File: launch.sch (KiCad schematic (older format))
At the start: 24 parts, among them J15 CHARGE_A, J16 CHARGE_B, Q1 Q_NPN_BCE, Q2 Q_NMOS_DGS, Q3 Q_NPN_BCE, Q4 Q_NMOS_DGS

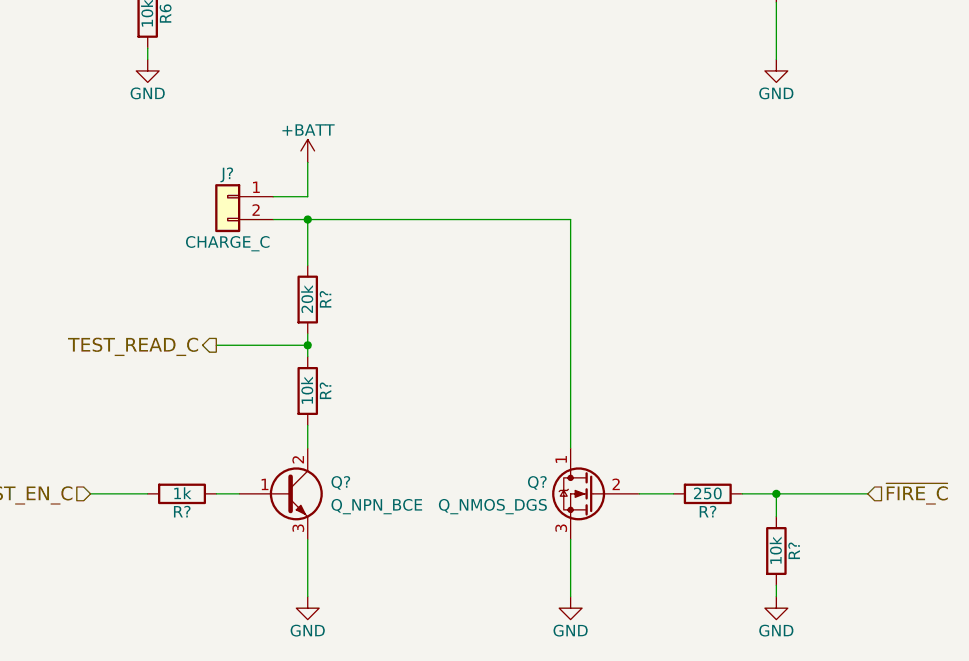
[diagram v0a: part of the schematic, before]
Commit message: added sd card
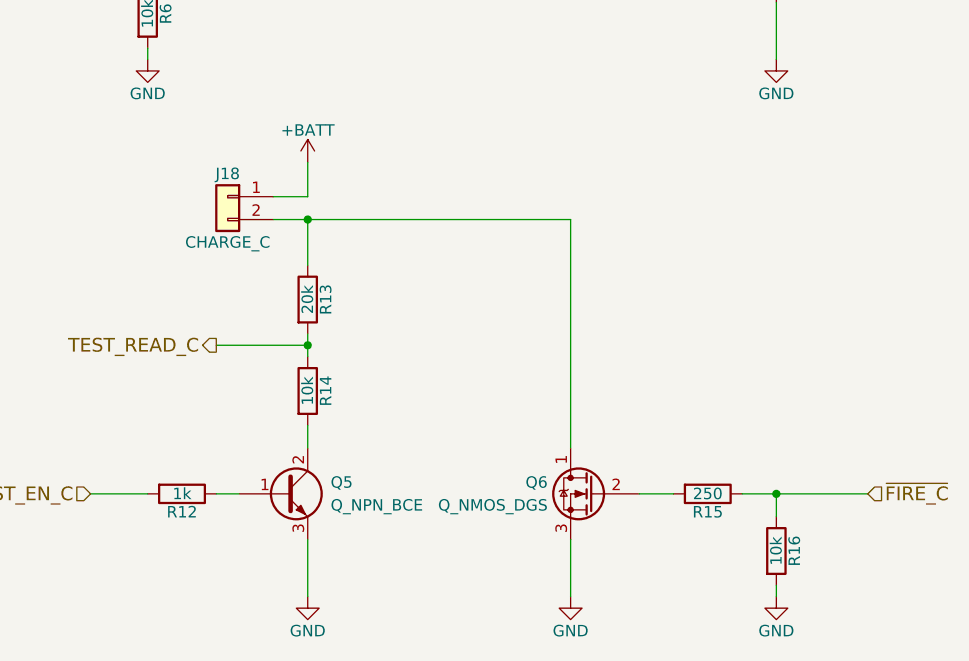
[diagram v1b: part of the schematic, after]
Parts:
- gave numbers to parts that had none: 8
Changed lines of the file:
@@
 LIBS:RFM95
 LIBS:TXB0104DR
+LIBS:LOGIC-TXS0108EPWR_TSSOP20_
 LIBS:Draco-cache
 EELAYER 25 0
@@
 $EndDescr
 $Comp
-L +BATT #PWR033
+L +BATT #PWR035
 U 1 1 5A5BE339
 P 2350 1600
-F 0 "#PWR033" H 2350 1450 50  0001 C CNN
+F 0 "#PWR035" H 2350 1450 50  0001 C CNN
 F 1 "+BATT" H 2350 1740 50  0000 C CNN
 F 2 "" H 2350 1600 50  0001 C CNN
@@
 $EndComp
 $Comp
-L GND #PWR034
+L GND #PWR036
 U 1 1 5A5BE533
 P 2350 3500
-F 0 "#PWR034" H 2350 3250 50  0001 C CNN
+F 0 "#PWR036" H 2350 3250 50  0001 C CNN
 F 1 "GND" H 2350 3350 50  0000 C CNN
 F 2 "" H 2350 3500 50  0001 C CNN
@@
 	3500 3250 3500 3500
 $Comp
-L GND #PWR035
+L GND #PWR037
 U 1 1 5A5BF84A
 P 3500 3500
-F 0 "#PWR035" H 3500 3250 50  0001 C CNN
+F 0 "#PWR037" H 3500 3250 50  0001 C CNN
 F 1 "GND" H 3500 3350 50  0000 C CNN
 F 2 "" H 3500 3500 50  0001 C CNN
@@
 $EndComp
 $Comp
-L GND #PWR036
+L GND #PWR038
 U 1 1 5A5BFA29
 P 4400 3500
-F 0 "#PWR036" H 4400 3250 50  0001 C CNN
+F 0 "#PWR038" H 4400 3250 50  0001 C CNN
 F 1 "GND" H 4400 3350 50  0000 C CNN
 F 2 "" H 4400 3500 50  0001 C CNN
@@
 ~FIRE_A
 $Comp
-L +BATT #PWR037
+L +BATT #PWR039
 U 1 1 5A5C03B4
 P 7150 1600
-F 0 "#PWR037" H 7150 1450 50  0001 C CNN
+F 0 "#PWR039" H 7150 1450 50  0001 C CNN
 F 1 "+BATT" H 7150 1740 50  0000 C CNN
 F 2 "" H 7150 1600 50  0001 C CNN
@@
 $EndComp
 $Comp
-L GND #PWR038
+L GND #PWR040
 U 1 1 5A5C03DC
 P 7150 3500
-F 0 "#PWR038" H 7150 3250 50  0001 C CNN
+F 0 "#PWR040" H 7150 3250 50  0001 C CNN
 F 1 "GND" H 7150 3350 50  0000 C CNN
 F 2 "" H 7150 3500 50  0001 C CNN
@@
 	8300 3250 8300 3500
 $Comp
-L GND #PWR039
+L GND #PWR041
 U 1 1 5A5C03F2
 P 8300 3500
-F 0 "#PWR039" H 8300 3250 50  0001 C CNN
+F 0 "#PWR041" H 8300 3250 50  0001 C CNN
 F 1 "GND" H 8300 3350 50  0000 C CNN
 F 2 "" H 8300 3500 50  0001 C CNN
@@
 $EndComp
 $Comp
-L GND #PWR040
+L GND #PWR042
 U 1 1 5A5C040E
 P 9200 3500
-F 0 "#PWR040" H 9200 3250 50  0001 C CNN
+F 0 "#PWR042" H 9200 3250 50  0001 C CNN
 F 1 "GND" H 9200 3350 50  0000 C CNN
 F 2 "" H 9200 3500 50  0001 C CNN
@@
 Connection ~ 9200 3050
 $Comp
-L +BATT #PWR041
+L +BATT #PWR043
 U 1 1 5A5C9AE9
 P 5100 3950
-F 0 "#PWR041" H 5100 3800 50  0001 C CNN
+F 0 "#PWR043" H 5100 3800 50  0001 C CNN
 F 1 "+BATT" H 5100 4090 50  0000 C CNN
 F 2 "" H 5100 3950 50  0001 C CNN
@@
 $EndComp
 $Comp
-L Conn_01x02 J?
+L Conn_01x02 J18
 U 1 1 5A5C9AEF
 P 4750 4100
-F 0 "J?" H 4750 4200 50  0000 C CNN
+F 0 "J18" H 4750 4200 50  0000 C CNN
 F 1 "CHARGE_C" H 4750 3900 50  0000 C CNN
 F 2 "" H 4750 4100 50  0001 C CNN
@@
 	4950 4200 6250 4200
 $Comp
-L R R?
+L R R13
 U 1 1 5A5C9AF9
 P 5100 4550
-F 0 "R?" V 5180 4550 50  0000 C CNN
+F 0 "R13" V 5180 4550 50  0000 C CNN
 F 1 "20k" V 5100 4550 50  0000 C CNN
 F 2 "" V 5030 4550 50  0001 C CNN
@@
 $EndComp
 $Comp
-L R R?
+L R R14
 U 1 1 5A5C9AFF
 P 5100 4950
-F 0 "R?" V 5180 4950 50  0000 C CNN
+F 0 "R14" V 5180 4950 50  0000 C CNN
 F 1 "10k" V 5100 4950 50  0000 C CNN
 F 2 "" V 5030 4950 50  0001 C CNN
@@
 $EndComp
 $Comp
-L R R?
+L R R12
 U 1 1 5A5C9B05
 P 4550 5400
-F 0 "R?" V 4630 5400 50  0000 C CNN
+F 0 "R12" V 4630 5400 50  0000 C CNN
 F 1 "1k" V 4550 5400 50  0000 C CNN
 F 2 "" V 4480 5400 50  0001 C CNN
@@
 $EndComp
 $Comp
-L Q_NPN_BCE Q?
+L Q_NPN_BCE Q5
 U 1 1 5A5C9B0B
 P 5000 5400
-F 0 "Q?" H 5200 5450 50  0000 L CNN
+F 0 "Q5" H 5200 5450 50  0000 L CNN
 F 1 "Q_NPN_BCE" H 5200 5350 50  0000 L CNN
 F 2 "" H 5200 5500 50  0001 C CNN
@@
 $EndComp
 $Comp
-L GND #PWR042
+L GND #PWR044
 U 1 1 5A5C9B11
 P 5100 5850
-F 0 "#PWR042" H 5100 5600 50  0001 C CNN
+F 0 "#PWR044" H 5100 5600 50  0001 C CNN
 F 1 "GND" H 5100 5700 50  0000 C CNN
 F 2 "" H 5100 5850 50  0001 C CNN
@@
 TEST_READ_C
 $Comp
-L Q_NMOS_DGS Q?
+L Q_NMOS_DGS Q6
 U 1 1 5A5C9B20
 P 6350 5400
-F 0 "Q?" H 6550 5450 50  0000 L CNN
+F 0 "Q6" H 6550 5450 50  0000 L CNN
 F 1 "Q_NMOS_DGS" H 6550 5350 50  0000 L CNN
 F 2 "" H 6550 5500 50  0001 C CNN
@@
 	6250 5600 6250 5850
 $Comp
-L GND #PWR043
+L GND #PWR045
 U 1 1 5A5C9B27
 P 6250 5850
-F 0 "#PWR043" H 6250 5600 50  0001 C CNN
+F 0 "#PWR045" H 6250 5600 50  0001 C CNN
 F 1 "GND" H 6250 5700 50  0000 C CNN
 F 2 "" H 6250 5850 50  0001 C CNN
@@
 Connection ~ 5100 4200
 $Comp
-L R R?
+L R R16
 U 1 1 5A5C9B2F
 P 7150 5650
-F 0 "R?" V 7230 5650 50  0000 C CNN
+F 0 "R16" V 7230 5650 50  0000 C CNN
 F 1 "10k" V 7150 5650 50  0000 C CNN
 F 2 "" V 7080 5650 50  0001 C CNN
@@
 $EndComp
 $Comp
-L GND #PWR044
+L GND #PWR046
 U 1 1 5A5C9B35
 P 7150 5850
-F 0 "#PWR044" H 7150 5600 50  0001 C CNN
+F 0 "#PWR046" H 7150 5600 50  0001 C CNN
 F 1 "GND" H 7150 5700 50  0000 C CNN
 F 2 "" H 7150 5850 50  0001 C CNN
@@
 	7150 5850 7150 5800
 $Comp
-L R R?
+L R R15
 U 1 1 5A5C9B3C
 P 6850 5400
-F 0 "R?" V 6930 5400 50  0000 C CNN
+F 0 "R15" V 6930 5400 50  0000 C CNN
 F 1 "250" V 6850 5400 50  0000 C CNN
 F 2 "" V 6780 5400 50  0001 C CNN

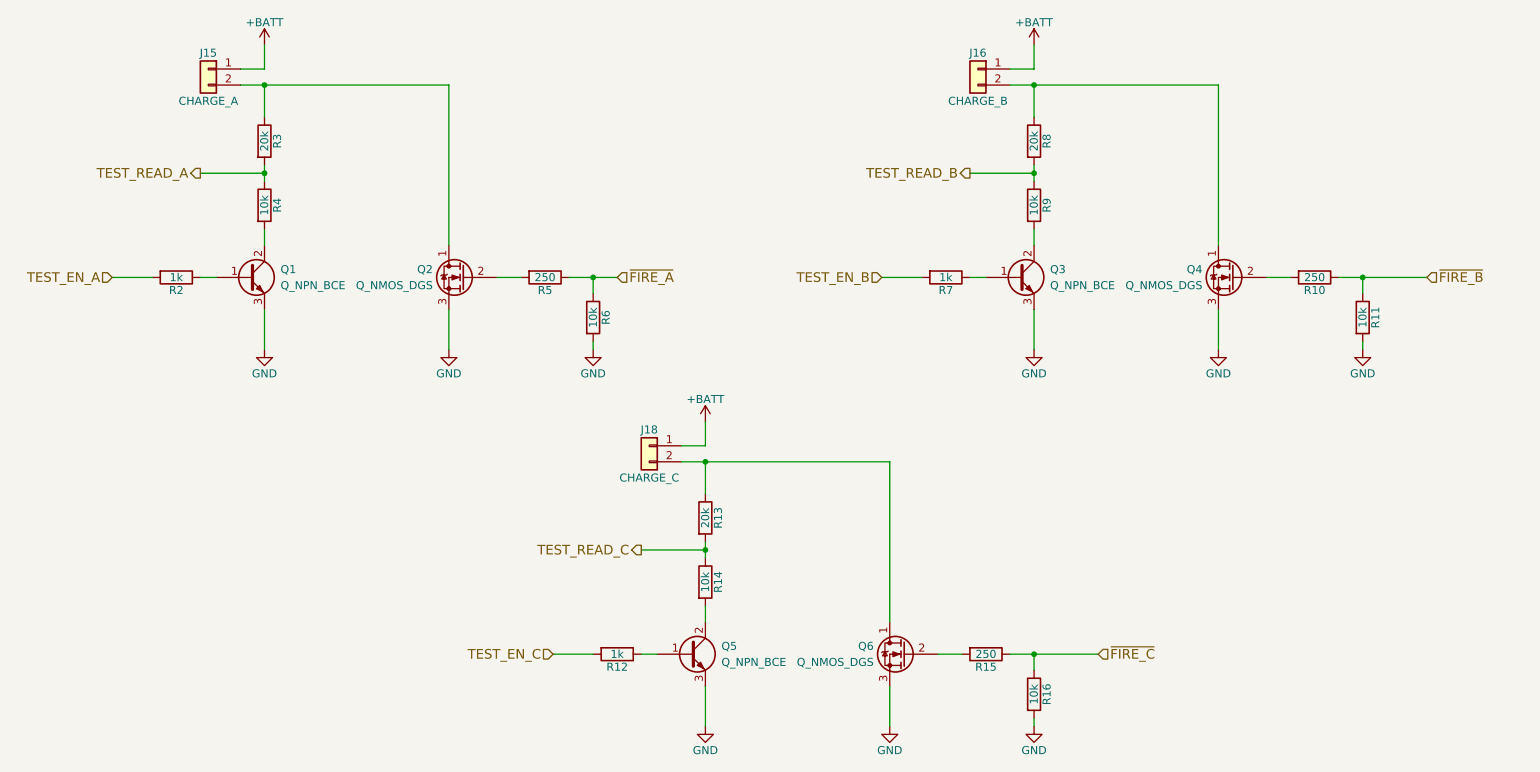
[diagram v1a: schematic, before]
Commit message: Did design review. Changed/confirmed voltage levels
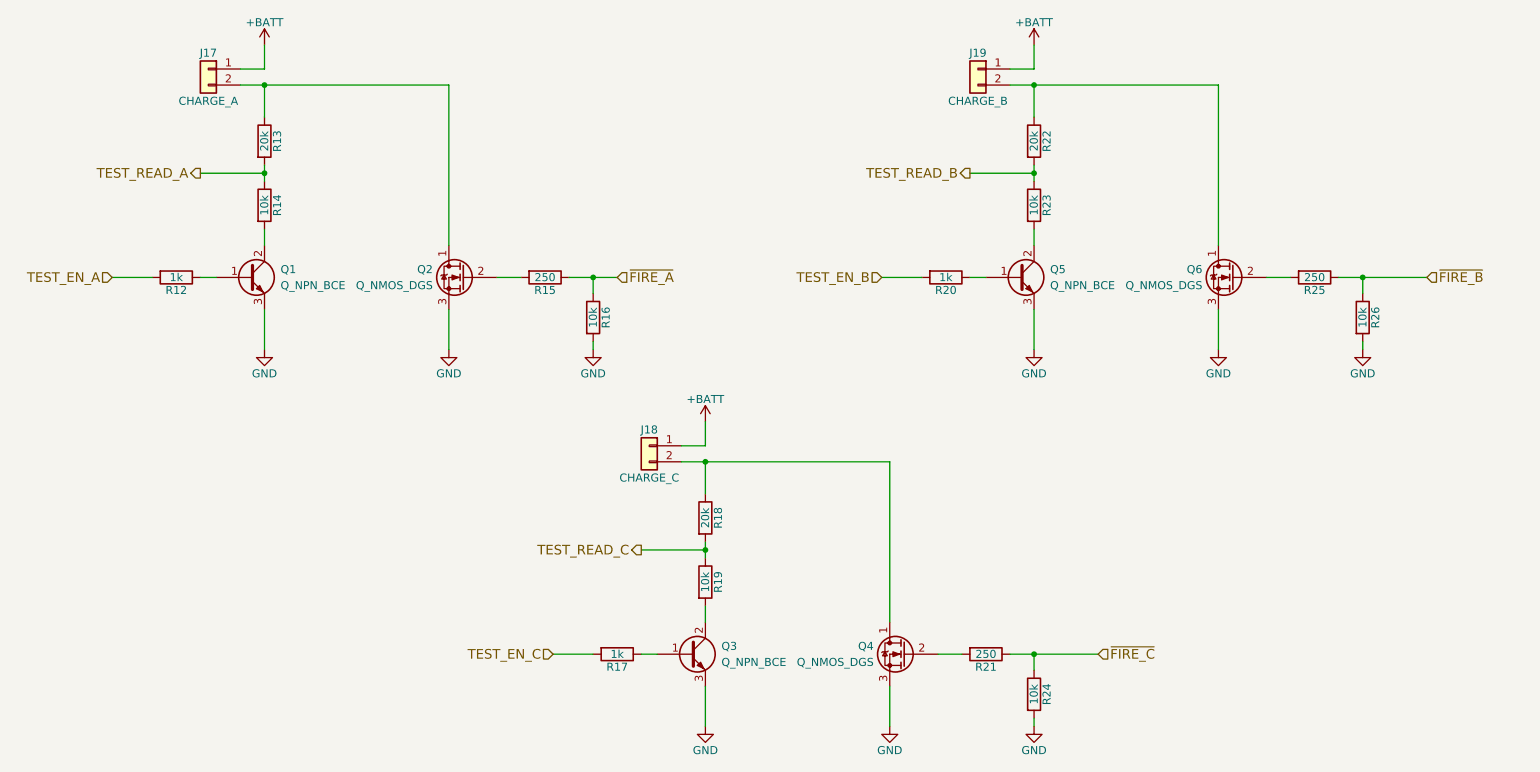
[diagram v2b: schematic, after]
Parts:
- R12: renamed from R2; footprint (none) -> Resistors_SMD:R_0805
- R13: renamed from R3; footprint (none) -> Resistors_SMD:R_0805
- R14: renamed from R4; footprint (none) -> Resistors_SMD:R_0805
- R15: renamed from R5; footprint (none) -> Resistors_SMD:R_0805
- R16: renamed from R6; footprint (none) -> Resistors_SMD:R_0805
- R17: renamed from R12; footprint (none) -> Resistors_SMD:R_0805
- R18: renamed from R13; footprint (none) -> Resistors_SMD:R_0805
- R19: renamed from R14; footprint (none) -> Resistors_SMD:R_0805
- R20: renamed from R7; footprint (none) -> Resistors_SMD:R_0805
- R21: renamed from R15; footprint (none) -> Resistors_SMD:R_0805
- R22: renamed from R8; footprint (none) -> Resistors_SMD:R_0805
- R23: renamed from R9; footprint (none) -> Resistors_SMD:R_0805
- R24: renamed from R16; footprint (none) -> Resistors_SMD:R_0805
- R25: renamed from R10; footprint (none) -> Resistors_SMD:R_0805
- R26: renamed from R11; footprint (none) -> Resistors_SMD:R_0805
- renumbered J15 to J17, J16 to J19, Q5 to Q3, Q6 to Q4, Q3 to Q5, Q4 to Q6
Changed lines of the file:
@@
 $EndDescr
 $Comp
-L +BATT #PWR035
+L +BATT #PWR046
 U 1 1 5A5BE339
 P 2350 1600
-F 0 "#PWR035" H 2350 1450 50  0001 C CNN
+F 0 "#PWR046" H 2350 1450 50  0001 C CNN
 F 1 "+BATT" H 2350 1740 50  0000 C CNN
 F 2 "" H 2350 1600 50  0001 C CNN
@@
 $EndComp
 $Comp
-L Conn_01x02 J15
+L Conn_01x02 J17
 U 1 1 5A5BE34D
 P 2000 1750
-F 0 "J15" H 2000 1850 50  0000 C CNN
+F 0 "J17" H 2000 1850 50  0000 C CNN
 F 1 "CHARGE_A" H 2000 1550 50  0000 C CNN
 F 2 "" H 2000 1750 50  0001 C CNN
@@
 	2200 1850 3500 1850
 $Comp
-L R R3
+L R R13
 U 1 1 5A5BE412
 P 2350 2200
-F 0 "R3" V 2430 2200 50  0000 C CNN
+F 0 "R13" V 2430 2200 50  0000 C CNN
 F 1 "20k" V 2350 2200 50  0000 C CNN
-F 2 "" V 2280 2200 50  0001 C CNN
+F 2 "Resistors_SMD:R_0805" V 2280 2200 50  0001 C CNN
 F 3 "" H 2350 2200 50  0001 C CNN
 	1    2350 2200
@@
 $EndComp
 $Comp
-L R R4
+L R R14
 U 1 1 5A5BE487
 P 2350 2600
-F 0 "R4" V 2430 2600 50  0000 C CNN
+F 0 "R14" V 2430 2600 50  0000 C CNN
 F 1 "10k" V 2350 2600 50  0000 C CNN
-F 2 "" V 2280 2600 50  0001 C CNN
+F 2 "Resistors_SMD:R_0805" V 2280 2600 50  0001 C CNN
 F 3 "" H 2350 2600 50  0001 C CNN
 	1    2350 2600
@@
 $EndComp
 $Comp
-L R R2
+L R R12
 U 1 1 5A5BE4BA
 P 1800 3050
-F 0 "R2" V 1880 3050 50  0000 C CNN
+F 0 "R12" V 1880 3050 50  0000 C CNN
 F 1 "1k" V 1800 3050 50  0000 C CNN
-F 2 "" V 1730 3050 50  0001 C CNN
+F 2 "Resistors_SMD:R_0805" V 1730 3050 50  0001 C CNN
 F 3 "" H 1800 3050 50  0001 C CNN
 	1    1800 3050
@@
 $EndComp
 $Comp
-L GND #PWR036
+L GND #PWR047
 U 1 1 5A5BE533
 P 2350 3500
-F 0 "#PWR036" H 2350 3250 50  0001 C CNN
+F 0 "#PWR047" H 2350 3250 50  0001 C CNN
 F 1 "GND" H 2350 3350 50  0000 C CNN
 F 2 "" H 2350 3500 50  0001 C CNN
@@
 	3500 3250 3500 3500
 $Comp
-L GND #PWR037
+L GND #PWR048
 U 1 1 5A5BF84A
 P 3500 3500
-F 0 "#PWR037" H 3500 3250 50  0001 C CNN
+F 0 "#PWR048" H 3500 3250 50  0001 C CNN
 F 1 "GND" H 3500 3350 50  0000 C CNN
 F 2 "" H 3500 3500 50  0001 C CNN
@@
 Connection ~ 2350 1850
 $Comp
-L R R6
+L R R16
 U 1 1 5A5BF9CA
 P 4400 3300
-F 0 "R6" V 4480 3300 50  0000 C CNN
+F 0 "R16" V 4480 3300 50  0000 C CNN
 F 1 "10k" V 4400 3300 50  0000 C CNN
-F 2 "" V 4330 3300 50  0001 C CNN
+F 2 "Resistors_SMD:R_0805" V 4330 3300 50  0001 C CNN
 F 3 "" H 4400 3300 50  0001 C CNN
 	1    4400 3300
@@
 $EndComp
 $Comp
-L GND #PWR038
+L GND #PWR049
 U 1 1 5A5BFA29
 P 4400 3500
-F 0 "#PWR038" H 4400 3250 50  0001 C CNN
+F 0 "#PWR049" H 4400 3250 50  0001 C CNN
 F 1 "GND" H 4400 3350 50  0000 C CNN
 F 2 "" H 4400 3500 50  0001 C CNN
@@
 	4400 3500 4400 3450
 $Comp
-L R R5
+L R R15
 U 1 1 5A5BFB6E
 P 4100 3050
-F 0 "R5" V 4180 3050 50  0000 C CNN
+F 0 "R15" V 4180 3050 50  0000 C CNN
 F 1 "250" V 4100 3050 50  0000 C CNN
-F 2 "" V 4030 3050 50  0001 C CNN
+F 2 "Resistors_SMD:R_0805" V 4030 3050 50  0001 C CNN
 F 3 "" H 4100 3050 50  0001 C CNN
 	1    4100 3050
@@
 ~FIRE_A
 $Comp
-L +BATT #PWR039
+L +BATT #PWR050
 U 1 1 5A5C03B4
 P 7150 1600
-F 0 "#PWR039" H 7150 1450 50  0001 C CNN
+F 0 "#PWR050" H 7150 1450 50  0001 C CNN
 F 1 "+BATT" H 7150 1740 50  0000 C CNN
 F 2 "" H 7150 1600 50  0001 C CNN
@@
 $EndComp
 $Comp
-L Conn_01x02 J16
+L Conn_01x02 J19
 U 1 1 5A5C03BA
 P 6800 1750
-F 0 "J16" H 6800 1850 50  0000 C CNN
+F 0 "J19" H 6800 1850 50  0000 C CNN
 F 1 "CHARGE_B" H 6800 1550 50  0000 C CNN
 F 2 "" H 6800 1750 50  0001 C CNN
@@
 	7000 1850 8300 1850
 $Comp
-L R R8
+L R R22
 U 1 1 5A5C03C4
 P 7150 2200
-F 0 "R8" V 7230 2200 50  0000 C CNN
+F 0 "R22" V 7230 2200 50  0000 C CNN
 F 1 "20k" V 7150 2200 50  0000 C CNN
-F 2 "" V 7080 2200 50  0001 C CNN
+F 2 "Resistors_SMD:R_0805" V 7080 2200 50  0001 C CNN
 F 3 "" H 7150 2200 50  0001 C CNN
 	1    7150 2200
@@
 $EndComp
 $Comp
-L R R9
+L R R23
 U 1 1 5A5C03CA
 P 7150 2600
-F 0 "R9" V 7230 2600 50  0000 C CNN
+F 0 "R23" V 7230 2600 50  0000 C CNN
 F 1 "10k" V 7150 2600 50  0000 C CNN
-F 2 "" V 7080 2600 50  0001 C CNN
+F 2 "Resistors_SMD:R_0805" V 7080 2600 50  0001 C CNN
 F 3 "" H 7150 2600 50  0001 C CNN
 	1    7150 2600
@@
 $EndComp
 $Comp
-L R R7
+L R R20
 U 1 1 5A5C03D0
 P 6600 3050
-F 0 "R7" V 6680 3050 50  0000 C CNN
+F 0 "R20" V 6680 3050 50  0000 C CNN
 F 1 "1k" V 6600 3050 50  0000 C CNN
-F 2 "" V 6530 3050 50  0001 C CNN
+F 2 "Resistors_SMD:R_0805" V 6530 3050 50  0001 C CNN
 F 3 "" H 6600 3050 50  0001 C CNN
 	1    6600 3050
@@
 $EndComp
 $Comp
-L Q_NPN_BCE Q3
+L Q_NPN_BCE Q5
 U 1 1 5A5C03D6
 P 7050 3050
-F 0 "Q3" H 7250 3100 50  0000 L CNN
+F 0 "Q5" H 7250 3100 50  0000 L CNN
 F 1 "Q_NPN_BCE" H 7250 3000 50  0000 L CNN
 F 2 "" H 7250 3150 50  0001 C CNN
@@
 $EndComp
 $Comp
-L GND #PWR040
+L GND #PWR051
 U 1 1 5A5C03DC
 P 7150 3500
-F 0 "#PWR040" H 7150 3250 50  0001 C CNN
+F 0 "#PWR051" H 7150 3250 50  0001 C CNN
 F 1 "GND" H 7150 3350 50  0000 C CNN
 F 2 "" H 7150 3500 50  0001 C CNN
@@
 TEST_READ_B
 $Comp
-L Q_NMOS_DGS Q4
+L Q_NMOS_DGS Q6
 U 1 1 5A5C03EB
 P 8400 3050
-F 0 "Q4" H 8600 3100 50  0000 L CNN
+F 0 "Q6" H 8600 3100 50  0000 L CNN
 F 1 "Q_NMOS_DGS" H 8600 3000 50  0000 L CNN
 F 2 "" H 8600 3150 50  0001 C CNN
@@
 	8300 3250 8300 3500
 $Comp
-L GND #PWR041
+L GND #PWR052
 U 1 1 5A5C03F2
 P 8300 3500
-F 0 "#PWR041" H 8300 3250 50  0001 C CNN
+F 0 "#PWR052" H 8300 3250 50  0001 C CNN
 F 1 "GND" H 8300 3350 50  0000 C CNN
 F 2 "" H 8300 3500 50  0001 C CNN
@@
 Connection ~ 7150 1850
 $Comp
-L R R11
+L R R26
 U 1 1 5A5C0408
 P 9200 3300
-F 0 "R11" V 9280 3300 50  0000 C CNN
+F 0 "R26" V 9280 3300 50  0000 C CNN
 F 1 "10k" V 9200 3300 50  0000 C CNN
-F 2 "" V 9130 3300 50  0001 C CNN
+F 2 "Resistors_SMD:R_0805" V 9130 3300 50  0001 C CNN
 F 3 "" H 9200 3300 50  0001 C CNN
 	1    9200 3300
@@
 $EndComp
 $Comp
-L GND #PWR042
+L GND #PWR053
 U 1 1 5A5C040E
 P 9200 3500
-F 0 "#PWR042" H 9200 3250 50  0001 C CNN
+F 0 "#PWR053" H 9200 3250 50  0001 C CNN
 F 1 "GND" H 9200 3350 50  0000 C CNN
 F 2 "" H 9200 3500 50  0001 C CNN
@@
 	9200 3500 9200 3450
 $Comp
-L R R10
+L R R25
 U 1 1 5A5C0415
 P 8900 3050
-F 0 "R10" V 8980 3050 50  0000 C CNN
+F 0 "R25" V 8980 3050 50  0000 C CNN
 F 1 "250" V 8900 3050 50  0000 C CNN
-F 2 "" V 8830 3050 50  0001 C CNN
+F 2 "Resistors_SMD:R_0805" V 8830 3050 50  0001 C CNN
 F 3 "" H 8900 3050 50  0001 C CNN
 	1    8900 3050
@@
 Connection ~ 9200 3050
 $Comp
-L +BATT #PWR043
+L +BATT #PWR054
 U 1 1 5A5C9AE9
 P 5100 3950
-F 0 "#PWR043" H 5100 3800 50  0001 C CNN
+F 0 "#PWR054" H 5100 3800 50  0001 C CNN
 F 1 "+BATT" H 5100 4090 50  0000 C CNN
 F 2 "" H 5100 3950 50  0001 C CNN
@@
 	4950 4200 6250 4200
 $Comp
-L R R13
+L R R18
 U 1 1 5A5C9AF9
 P 5100 4550
-F 0 "R13" V 5180 4550 50  0000 C CNN
+F 0 "R18" V 5180 4550 50  0000 C CNN
 F 1 "20k" V 5100 4550 50  0000 C CNN
-F 2 "" V 5030 4550 50  0001 C CNN
+F 2 "Resistors_SMD:R_0805" V 5030 4550 50  0001 C CNN
 F 3 "" H 5100 4550 50  0001 C CNN
 	1    5100 4550
@@
 $EndComp
 $Comp
-L R R14
+L R R19
 U 1 1 5A5C9AFF
 P 5100 4950
-F 0 "R14" V 5180 4950 50  0000 C CNN
+F 0 "R19" V 5180 4950 50  0000 C CNN
 F 1 "10k" V 5100 4950 50  0000 C CNN
-F 2 "" V 5030 4950 50  0001 C CNN
+F 2 "Resistors_SMD:R_0805" V 5030 4950 50  0001 C CNN
 F 3 "" H 5100 4950 50  0001 C CNN
 	1    5100 4950
@@
 $EndComp
 $Comp
-L R R12
+L R R17
 U 1 1 5A5C9B05
 P 4550 5400
-F 0 "R12" V 4630 5400 50  0000 C CNN
+F 0 "R17" V 4630 5400 50  0000 C CNN
 F 1 "1k" V 4550 5400 50  0000 C CNN
-F 2 "" V 4480 5400 50  0001 C CNN
+F 2 "Resistors_SMD:R_0805" V 4480 5400 50  0001 C CNN
 F 3 "" H 4550 5400 50  0001 C CNN
 	1    4550 5400
@@
 $EndComp
 $Comp
-L Q_NPN_BCE Q5
+L Q_NPN_BCE Q3
 U 1 1 5A5C9B0B
 P 5000 5400
-F 0 "Q5" H 5200 5450 50  0000 L CNN
+F 0 "Q3" H 5200 5450 50  0000 L CNN
 F 1 "Q_NPN_BCE" H 5200 5350 50  0000 L CNN
 F 2 "" H 5200 5500 50  0001 C CNN
@@
 $EndComp
 $Comp
-L GND #PWR044
+L GND #PWR055
 U 1 1 5A5C9B11
 P 5100 5850
-F 0 "#PWR044" H 5100 5600 50  0001 C CNN
+F 0 "#PWR055" H 5100 5600 50  0001 C CNN
 F 1 "GND" H 5100 5700 50  0000 C CNN
 F 2 "" H 5100 5850 50  0001 C CNN
@@
 TEST_READ_C
 $Comp
-L Q_NMOS_DGS Q6
+L Q_NMOS_DGS Q4
 U 1 1 5A5C9B20
 P 6350 5400
-F 0 "Q6" H 6550 5450 50  0000 L CNN
+F 0 "Q4" H 6550 5450 50  0000 L CNN
 F 1 "Q_NMOS_DGS" H 6550 5350 50  0000 L CNN
 F 2 "" H 6550 5500 50  0001 C CNN
@@
 	6250 5600 6250 5850
 $Comp
-L GND #PWR045
+L GND #PWR056
 U 1 1 5A5C9B27
 P 6250 5850
-F 0 "#PWR045" H 6250 5600 50  0001 C CNN
+F 0 "#PWR056" H 6250 5600 50  0001 C CNN
 F 1 "GND" H 6250 5700 50  0000 C CNN
 F 2 "" H 6250 5850 50  0001 C CNN
@@
 Connection ~ 5100 4200
 $Comp
-L R R16
+L R R24
 U 1 1 5A5C9B2F
 P 7150 5650
-F 0 "R16" V 7230 5650 50  0000 C CNN
+F 0 "R24" V 7230 5650 50  0000 C CNN
 F 1 "10k" V 7150 5650 50  0000 C CNN
-F 2 "" V 7080 5650 50  0001 C CNN
+F 2 "Resistors_SMD:R_0805" V 7080 5650 50  0001 C CNN
 F 3 "" H 7150 5650 50  0001 C CNN
 	1    7150 5650
@@
 $EndComp
 $Comp
-L GND #PWR046
+L GND #PWR057
 U 1 1 5A5C9B35
 P 7150 5850
-F 0 "#PWR046" H 7150 5600 50  0001 C CNN
+F 0 "#PWR057" H 7150 5600 50  0001 C CNN
 F 1 "GND" H 7150 5700 50  0000 C CNN
 F 2 "" H 7150 5850 50  0001 C CNN
@@
 	7150 5850 7150 5800
 $Comp
-L R R15
+L R R21
 U 1 1 5A5C9B3C
 P 6850 5400
-F 0 "R15" V 6930 5400 50  0000 C CNN
+F 0 "R21" V 6930 5400 50  0000 C CNN
 F 1 "250" V 6850 5400 50  0000 C CNN
-F 2 "" V 6780 5400 50  0001 C CNN
+F 2 "Resistors_SMD:R_0805" V 6780 5400 50  0001 C CNN
 F 3 "" H 6850 5400 50  0001 C CNN
 	1    6850 5400
